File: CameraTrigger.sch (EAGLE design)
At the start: 29 parts, among them J1 3p-2.54, J2 3p-2.54, J3 3p-2.54, J4 3p-2.54, J5 3p-2.54, J6 3p-2.54, J7 3p-2.54, J8 3p-2.54, M1 ARDUINO_R3_ICSP, U2 PCF8574_PW_20, U3 DC-DC Switching, U4 MCP73831T-2ACI/OT

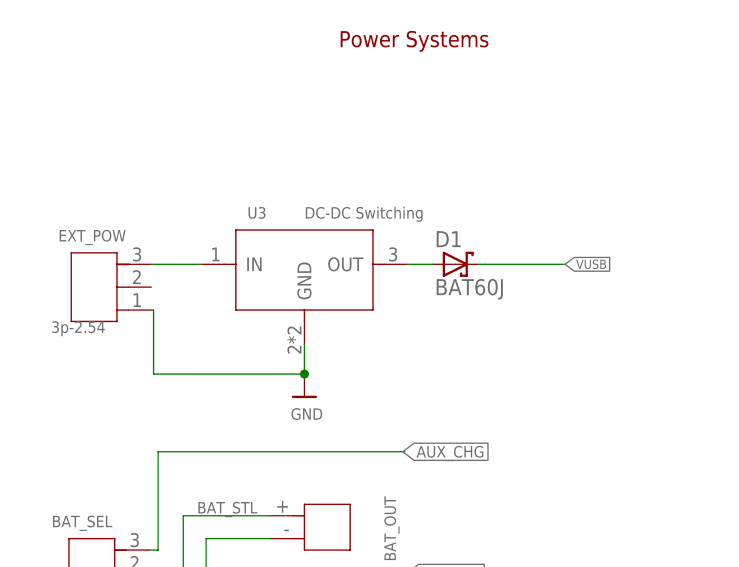
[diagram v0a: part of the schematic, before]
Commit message: Replace voltage regulator with DC-DC switchmode
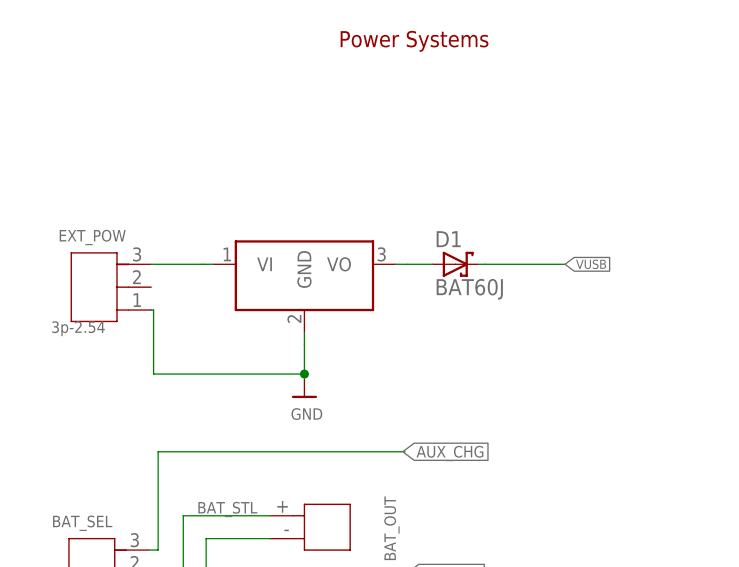
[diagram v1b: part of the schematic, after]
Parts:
- removed U3: DC-DC Switching, Seeed-OPL-ic:PMIC-L7805CV-DG(TO-220)
- added OKI-78SR-5: DCDC_OKI-78SR, carrilib:DCDC_OKI-78SR
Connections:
- net GND: now also OKI-78SR-5.GND; no longer U3.GND
- net N$2: now also OKI-78SR-5.VO; no longer U3.OUT
- net VEXT: now also OKI-78SR-5.VI; no longer U3.IN
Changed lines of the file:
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@@
 <part name="U2" library="PCF8574" deviceset="PCF8574_PW_20" device=""/>
 <part name="JP1" library="pinhead" deviceset="PINHD-1X7" device="" value="KEYPAD"/>
-<part name="U3" library="Seeed-OPL-ic" deviceset="PMIC-L7805CV-DG(TO-220)" device="" value="DC-DC Switching"/>
 <part name="BAT_OUT" library="Seeed-OPL-Connector" deviceset="DIP-JST-2P-2.0" device="" value="2p-2.0"/>
 <part name="BAT_IN" library="Seeed-OPL-Connector" deviceset="DIP-JST-2P-2.0" device="" value="2p-2.0"/>
@@
 <part name="M1" library="adafruit" deviceset="ARDUINO_R3_ICSP" device=""/>
 <part name="D1" library="diode" deviceset="BAT60J" device=""/>
+<part name="OKI-78SR-5" library="carrilib" deviceset="DCDC_OKI-78SR" device=""/>
 </parts>
 <sheets>
@@
 <instance part="U2" gate="A" x="175.26" y="165.1"/>
 <instance part="JP1" gate="A" x="251.46" y="152.4" rot="MR180"/>
-<instance part="U3" gate="G$1" x="31.75" y="67.31"/>
 <instance part="BAT_OUT" gate="G$1" x="30.48" y="38.1" smashed="yes">
 <attribute name="NAME" x="41.91" y="34.29" size="1.27" layer="95" ratio="10" rot="R90"/>
@@
 <instance part="M1" gate="G$1" x="10.16" y="116.84"/>
 <instance part="D1" gate="G$1" x="48.514" y="67.31"/>
+<instance part="OKI-78SR-5" gate="G$1" x="29.21" y="67.31"/>
 </instances>
 <busses>
@@
 </segment>
 <segment>
-<pinref part="U3" gate="G$1" pin="GND"/>
 <wire x1="31.75" y1="55.118" x2="31.75" y2="58.42" width="0.1524" layer="91"/>
 <junction x="31.75" y="55.118"/>
@@
 <wire x1="14.986" y1="62.23" x2="14.986" y2="55.118" width="0.1524" layer="91"/>
 <wire x1="31.75" y1="55.118" x2="14.986" y2="55.118" width="0.1524" layer="91"/>
+<pinref part="OKI-78SR-5" gate="G$1" pin="GND"/>
+<wire x1="31.75" y1="59.69" x2="31.75" y2="58.42" width="0.1524" layer="91"/>
 </segment>
 <segment>
@@
 <net name="VEXT" class="1">
 <segment>
-<pinref part="U3" gate="G$1" pin="IN"/>
 <pinref part="EXT_POW" gate="G$1" pin="P$3"/>
 <wire x1="20.32" y1="67.31" x2="14.732" y2="67.31" width="0.1524" layer="91"/>
+<pinref part="OKI-78SR-5" gate="G$1" pin="VI"/>
+<wire x1="21.59" y1="67.31" x2="20.574" y2="67.31" width="0.1524" layer="91"/>
+<wire x1="20.574" y1="67.31" x2="20.32" y2="67.31" width="0.1524" layer="91"/>
 </segment>
 </net>
@@
 <net name="N$2" class="1">
 <segment>
-<pinref part="U3" gate="G$1" pin="OUT"/>
 <wire x1="43.18" y1="67.31" x2="45.974" y2="67.31" width="0.1524" layer="91"/>
 <pinref part="D1" gate="G$1" pin="A"/>
-</segment>
-</net>
+<pinref part="OKI-78SR-5" gate="G$1" pin="VO"/>
+<wire x1="41.91" y1="67.31" x2="43.18" y2="67.31" width="0.1524" layer="91"/>
+</segment>
+</net>
